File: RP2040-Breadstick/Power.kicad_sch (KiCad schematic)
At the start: 6 parts

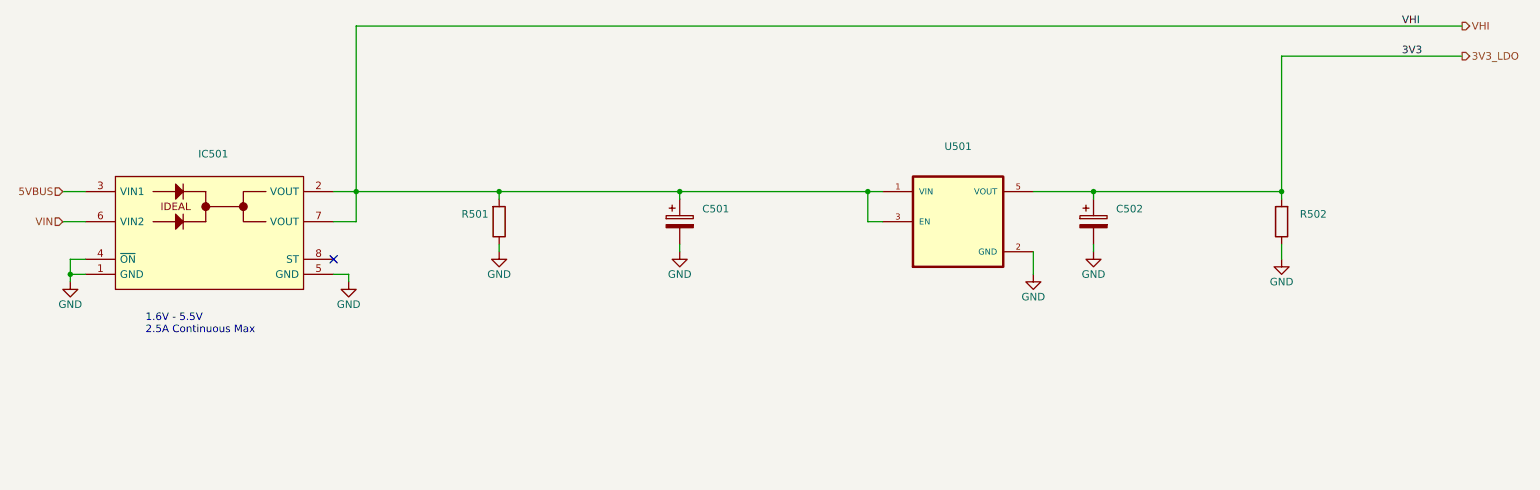
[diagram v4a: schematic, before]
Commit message: Created BOM spreadsheet
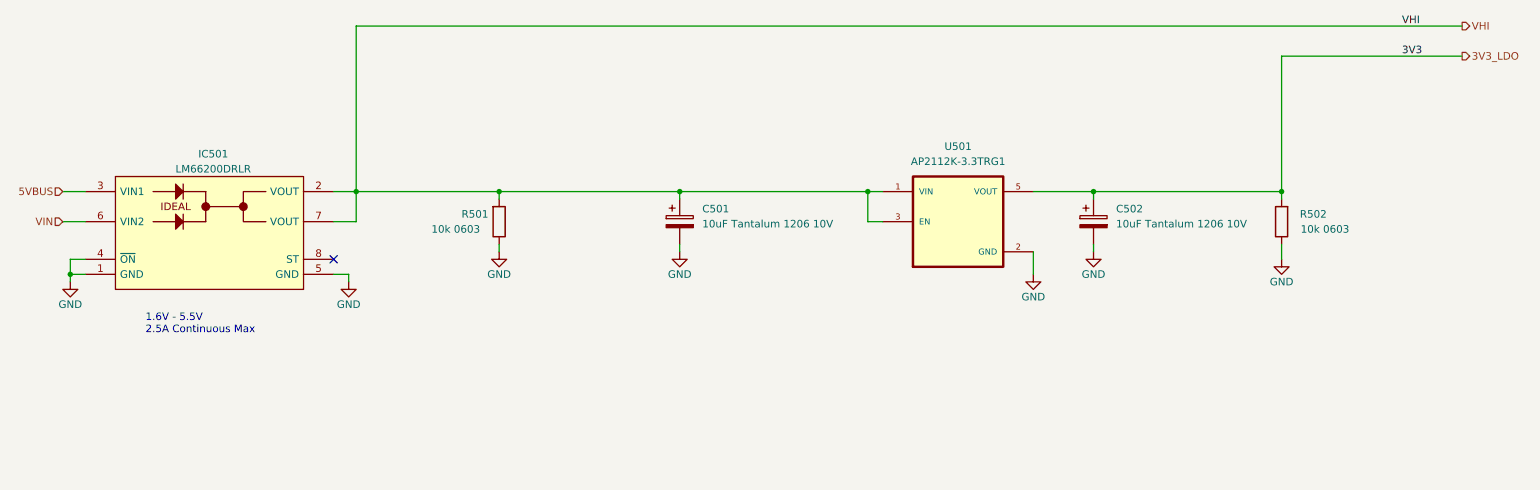
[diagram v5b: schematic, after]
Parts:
- C501, C502: value (none) -> 10uF Tantalum 1206 10V; footprint (none) -> T491A106K010AT:T491A106K010AT
- IC501: value (none) -> LM66200DRLR; footprint (none) -> SOTFL50P160X60-8L
- R501, R502: value (none) -> 10k 0603; footprint (none) -> Resistor_SMD:R_0603_1608Metric
- U501: value (none) -> AP2112K-3.3TRG1; footprint (none) -> AP2112K-3:SOT95P285X140-5N
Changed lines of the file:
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@@
       (effects (font (size 1.27 1.27)) (justify left))
     )
-    (property "Value" "" (id 1) (at 245.11 82.55 0)
-      (effects (font (size 1.27 1.27)) (justify left))
-    )
-    (property "Footprint" "" (id 2) (at 235.458 81.28 90)
+    (property "Value" "10k 0603" (id 1) (at 245.11 82.55 0)
+      (effects (font (size 1.27 1.27)) (justify left))
+    )
+    (property "Footprint" "Resistor_SMD:R_0603_1608Metric" (id 2) (at 235.458 81.28 90)
       (effects (font (size 1.27 1.27)) hide)
     )
@@
     (in_bom yes) (on_board yes)
     (property "Reference" "IC501" (id 0) (at 53.34 69.85 0))
-    (property "Value" "" (id 1) (at 53.34 72.39 0))
-    (property "Footprint" "" (id 2) (at 82.55 81.28 0)
+    (property "Value" "LM66200DRLR" (id 1) (at 53.34 72.39 0))
+    (property "Footprint" "SOTFL50P160X60-8L" (id 2) (at 82.55 81.28 0)
       (effects (font (size 1.27 1.27)) (justify left) hide)
     )
@@
       (effects (font (size 1.27 1.27)) (justify left))
     )
-    (property "Value" "" (id 1) (at 205.74 81.6609 0)
-      (effects (font (size 1.27 1.27)) (justify left))
-    )
-    (property "Footprint" "" (id 2) (at 202.8952 85.09 0)
+    (property "Value" "10uF Tantalum 1206 10V" (id 1) (at 205.74 81.6609 0)
+      (effects (font (size 1.27 1.27)) (justify left))
+    )
+    (property "Footprint" "T491A106K010AT:T491A106K010AT" (id 2) (at 202.8952 85.09 0)
       (effects (font (size 1.27 1.27)) hide)
     )
@@
       (effects (font (size 1.27 1.27)) (justify left))
     )
-    (property "Value" "" (id 1) (at 135.89 81.6609 0)
-      (effects (font (size 1.27 1.27)) (justify left))
-    )
-    (property "Footprint" "" (id 2) (at 133.0452 85.09 0)
+    (property "Value" "10uF Tantalum 1206 10V" (id 1) (at 135.89 81.6609 0)
+      (effects (font (size 1.27 1.27)) (justify left))
+    )
+    (property "Footprint" "T491A106K010AT:T491A106K010AT" (id 2) (at 133.0452 85.09 0)
       (effects (font (size 1.27 1.27)) hide)
     )
@@
     (in_bom yes) (on_board yes) (fields_autoplaced)
     (property "Reference" "U501" (id 0) (at 179.07 68.58 0))
-    (property "Value" "" (id 1) (at 179.07 71.12 0))
-    (property "Footprint" "" (id 2) (at 179.07 81.28 0)
+    (property "Value" "AP2112K-3.3TRG1" (id 1) (at 179.07 71.12 0))
+    (property "Footprint" "AP2112K-3:SOT95P285X140-5N" (id 2) (at 179.07 81.28 0)
       (effects (font (size 1.27 1.27)) (justify bottom) hide)
     )
@@
       (effects (font (size 1.27 1.27)) (justify left))
     )
-    (property "Value" "" (id 1) (at 90.17 82.55 0)
-      (effects (font (size 1.27 1.27)) (justify left))
-    )
-    (property "Footprint" "" (id 2) (at 99.822 81.28 90)
-      (effects (font (size 1.27 1.27)) hide)
-    )
+    (property "Value" "10k 0603" (id 1) (at 90.17 82.55 0)
+      (effects (font (size 1.27 1.27)) (justify left))
+    )
+    (property "Footprint" "Resistor_SMD:R_0603_1608Metric" (id 2) (at 99.822 81.28 90)
+      (effects (font (size 1.27 1.27)) hide)
+    )

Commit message: Updated crystal caps part numbers in BOM from 0201 to 0603
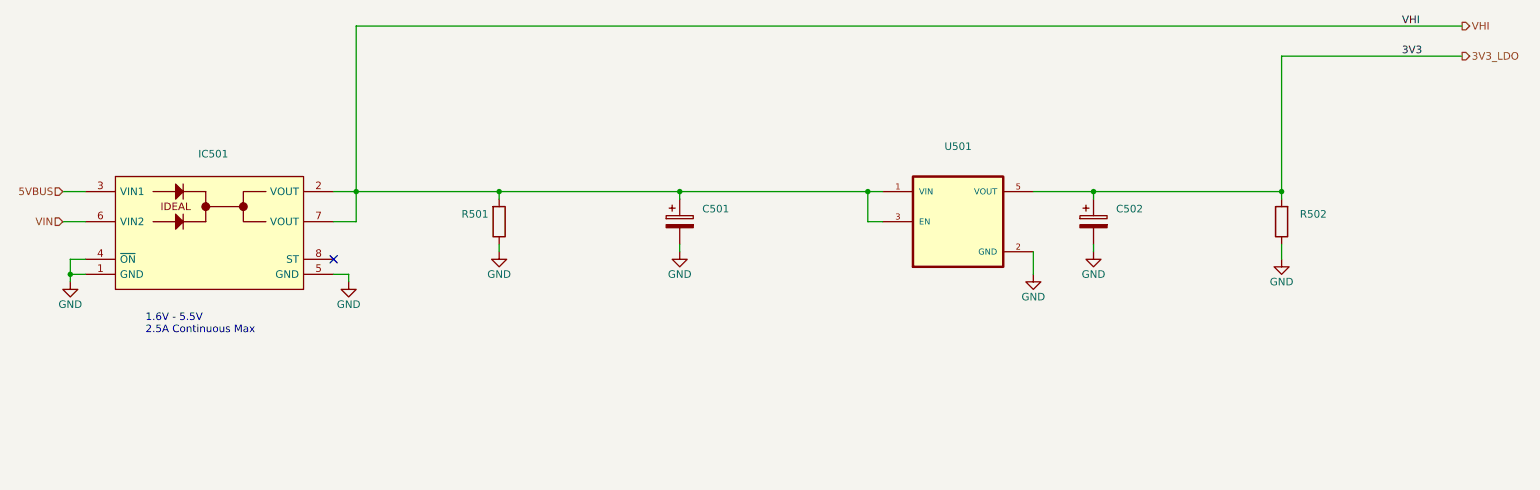
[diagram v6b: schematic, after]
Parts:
- C501, C502: value 10uF Tantalum 1206 10V -> (none); footprint T491A106K010AT:T491A106K010AT -> (none)
- IC501: value LM66200DRLR -> (none); footprint SOTFL50P160X60-8L -> (none)
- R501, R502: value 10k 0603 -> (none); footprint Resistor_SMD:R_0603_1608Metric -> (none)
- U501: value AP2112K-3.3TRG1 -> (none); footprint AP2112K-3:SOT95P285X140-5N -> (none)
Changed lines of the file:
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@@
       (effects (font (size 1.27 1.27)) (justify left))
     )
-    (property "Value" "10k 0603" (id 1) (at 245.11 82.55 0)
-      (effects (font (size 1.27 1.27)) (justify left))
-    )
-    (property "Footprint" "Resistor_SMD:R_0603_1608Metric" (id 2) (at 235.458 81.28 90)
+    (property "Value" "" (id 1) (at 245.11 82.55 0)
+      (effects (font (size 1.27 1.27)) (justify left))
+    )
+    (property "Footprint" "" (id 2) (at 235.458 81.28 90)
       (effects (font (size 1.27 1.27)) hide)
     )
@@
     (in_bom yes) (on_board yes)
     (property "Reference" "IC501" (id 0) (at 53.34 69.85 0))
-    (property "Value" "LM66200DRLR" (id 1) (at 53.34 72.39 0))
-    (property "Footprint" "SOTFL50P160X60-8L" (id 2) (at 82.55 81.28 0)
+    (property "Value" "" (id 1) (at 53.34 72.39 0))
+    (property "Footprint" "" (id 2) (at 82.55 81.28 0)
       (effects (font (size 1.27 1.27)) (justify left) hide)
     )
@@
       (effects (font (size 1.27 1.27)) (justify left))
     )
-    (property "Value" "10uF Tantalum 1206 10V" (id 1) (at 205.74 81.6609 0)
-      (effects (font (size 1.27 1.27)) (justify left))
-    )
-    (property "Footprint" "T491A106K010AT:T491A106K010AT" (id 2) (at 202.8952 85.09 0)
+    (property "Value" "" (id 1) (at 205.74 81.6609 0)
+      (effects (font (size 1.27 1.27)) (justify left))
+    )
+    (property "Footprint" "" (id 2) (at 202.8952 85.09 0)
       (effects (font (size 1.27 1.27)) hide)
     )
@@
       (effects (font (size 1.27 1.27)) (justify left))
     )
-    (property "Value" "10uF Tantalum 1206 10V" (id 1) (at 135.89 81.6609 0)
-      (effects (font (size 1.27 1.27)) (justify left))
-    )
-    (property "Footprint" "T491A106K010AT:T491A106K010AT" (id 2) (at 133.0452 85.09 0)
+    (property "Value" "" (id 1) (at 135.89 81.6609 0)
+      (effects (font (size 1.27 1.27)) (justify left))
+    )
+    (property "Footprint" "" (id 2) (at 133.0452 85.09 0)
       (effects (font (size 1.27 1.27)) hide)
     )
@@
     (in_bom yes) (on_board yes) (fields_autoplaced)
     (property "Reference" "U501" (id 0) (at 179.07 68.58 0))
-    (property "Value" "AP2112K-3.3TRG1" (id 1) (at 179.07 71.12 0))
-    (property "Footprint" "AP2112K-3:SOT95P285X140-5N" (id 2) (at 179.07 81.28 0)
+    (property "Value" "" (id 1) (at 179.07 71.12 0))
+    (property "Footprint" "" (id 2) (at 179.07 81.28 0)
       (effects (font (size 1.27 1.27)) (justify bottom) hide)
     )
@@
       (effects (font (size 1.27 1.27)) (justify left))
     )
-    (property "Value" "10k 0603" (id 1) (at 90.17 82.55 0)
-      (effects (font (size 1.27 1.27)) (justify left))
-    )
-    (property "Footprint" "Resistor_SMD:R_0603_1608Metric" (id 2) (at 99.822 81.28 90)
-      (effects (font (size 1.27 1.27)) hide)
-    )
+    (property "Value" "" (id 1) (at 90.17 82.55 0)
+      (effects (font (size 1.27 1.27)) (justify left))
+    )
+    (property "Footprint" "" (id 2) (at 99.822 81.28 90)
+      (effects (font (size 1.27 1.27)) hide)
+    )

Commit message: Swapped Tantalum Caps for MLCC, added CE, UKCA, RoHS symbols
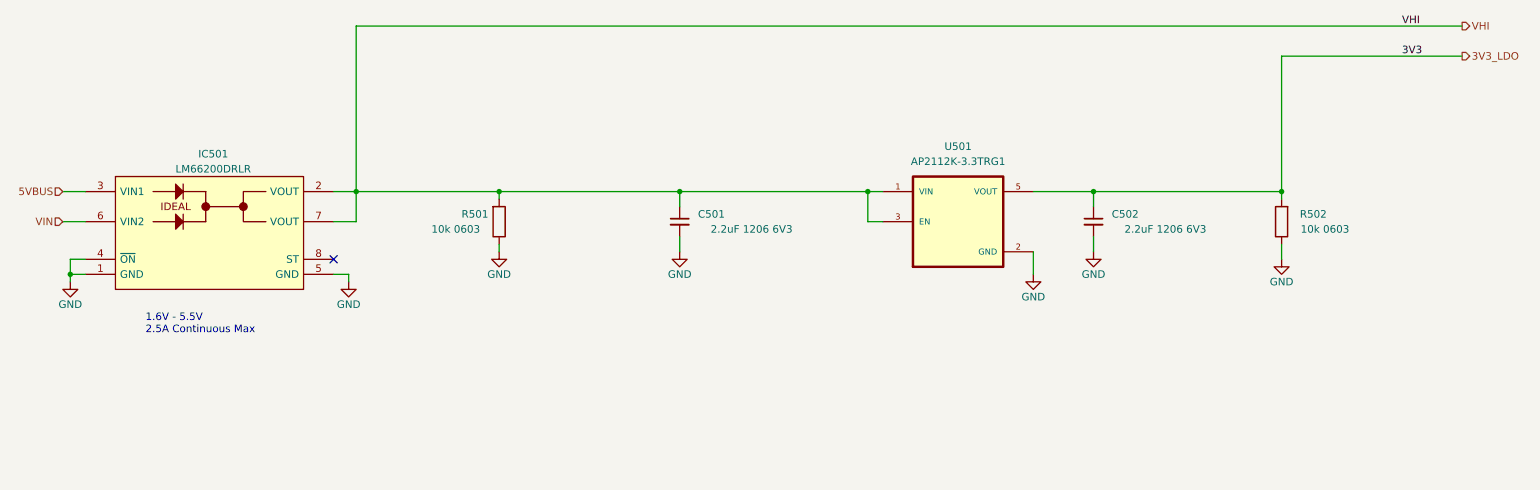
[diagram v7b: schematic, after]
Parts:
- removed C501, C502: (no value), symbol Device:C_Polarized
- added C501, C502: 2.2uF 1206 6V3, Capacitor_SMD:C_1206_3216Metric, symbol Device:C_Small
- IC501: value (none) -> LM66200DRLR; footprint (none) -> SOTFL50P160X60-8L
- R501, R502: value (none) -> 10k 0603; footprint (none) -> Resistor_SMD:R_0603_1608Metric
- U501: value (none) -> AP2112K-3.3TRG1; footprint (none) -> AP2112K-3:SOT95P285X140-5N
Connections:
- net 3V3_LDO: now also C502.1
- net GND: now also C501.2, C502.2
- net VHI: now also C501.1
